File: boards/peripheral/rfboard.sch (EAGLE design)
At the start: 30 parts, among them Q1 IRLML5203, Q2 IRLML5203, Q3 IRLML5203, Q4 IRLML5203, Q5 IRLML5203

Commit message: Changing boards for fet and text improvements
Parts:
- removed Q5: IRLML5203, ngohara_parts:IRLML5203
- removed RGS: 2.2k, resistor:R-US_R0805
- removed RIN: 10k, resistor:R-US_R0805
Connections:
- removed net N$2: Q5.G, RGS.1, RIN.2
- net AMB_ON: no longer RIN.1
- net GND: no longer Q5.S, RGS.2
- net N_GND: no longer Q5.D
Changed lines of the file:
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@@
 <part name="U$1" library="jst-ph" deviceset="JST-PH10-SMD" device=""/>
 <part name="U$3" library="jst-ph" deviceset="JST-PH10-SMD" device=""/>
-<part name="Q5" library="ngohara_parts" deviceset="IRLML5203" device=""/>
 <part name="X1" library="con-molex-micro-fit-3_0" deviceset="HEADER_POS4_?" device="43045-0406"/>
-<part name="RIN" library="resistor" deviceset="R-US_" device="R0805" value="10k"/>
-<part name="RGS" library="resistor" deviceset="R-US_" device="R0805" value="2.2k"/>
 </parts>
 <sheets>
@@
 <instance part="U$1" gate="G$1" x="81.28" y="58.42" rot="MR180"/>
 <instance part="U$3" gate="G$1" x="53.34" y="55.88"/>
-<instance part="Q5" gate="G$1" x="137.16" y="104.14" smashed="yes" rot="R90">
-<attribute name="NAME" x="139.7" y="111.76" size="1.778" layer="95" rot="R180"/>
-</instance>
 <instance part="X1" gate="G$1" x="2.54" y="58.42" rot="R180"/>
-<instance part="RIN" gate="G$1" x="127" y="101.6"/>
-<instance part="RGS" gate="G$1" x="142.24" y="99.06"/>
 </instances>
 <busses>
@@
 </segment>
 <segment>
-<pinref part="Q5" gate="G$1" pin="S"/>
 <pinref part="GND10" gate="1" pin="GND"/>
-<wire x1="142.24" y1="106.68" x2="149.86" y2="106.68" width="0.1524" layer="91"/>
 <junction x="154.94" y="106.68"/>
-<junction x="142.24" y="106.68"/>
-<pinref part="RGS" gate="G$1" pin="2"/>
 <wire x1="149.86" y1="106.68" x2="154.94" y2="106.68" width="0.1524" layer="91"/>
-<wire x1="147.32" y1="99.06" x2="149.86" y2="99.06" width="0.1524" layer="91"/>
-<wire x1="149.86" y1="99.06" x2="149.86" y2="106.68" width="0.1524" layer="91"/>
-<junction x="147.32" y="99.06"/>
-<junction x="149.86" y="106.68"/>
 </segment>
 </net>
@@
 <wire x1="121.92" y1="101.6" x2="119.38" y2="101.6" width="0.1524" layer="91"/>
 <junction x="119.38" y="101.6"/>
-<pinref part="RIN" gate="G$1" pin="1"/>
-</segment>
-</net>
-<net name="N$2" class="0">
-<segment>
-<pinref part="Q5" gate="G$1" pin="G"/>
-<pinref part="RIN" gate="G$1" pin="2"/>
-<wire x1="132.08" y1="101.6" x2="134.62" y2="101.6" width="0.1524" layer="91"/>
-<wire x1="134.62" y1="101.6" x2="134.62" y2="99.06" width="0.1524" layer="91"/>
-<pinref part="RGS" gate="G$1" pin="1"/>
-<wire x1="134.62" y1="99.06" x2="137.16" y2="99.06" width="0.1524" layer="91"/>
-<junction x="134.62" y="101.6"/>
-<junction x="132.08" y="101.6"/>
-<junction x="137.16" y="99.06"/>
 </segment>
 </net>
@@
 <junction x="134.62" y="119.38"/>
 <junction x="149.86" y="124.46"/>
-<pinref part="Q5" gate="G$1" pin="D"/>
 <wire x1="132.08" y1="111.76" x2="132.08" y2="106.68" width="0.1524" layer="91"/>
-<junction x="132.08" y="106.68"/>
 <wire x1="147.32" y1="83.82" x2="165.1" y2="83.82" width="0.1524" layer="91"/>
 <wire x1="165.1" y1="83.82" x2="165.1" y2="111.76" width="0.1524" layer="91"/>

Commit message: fixed improper ground issue
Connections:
- removed net N_GND: AMB2.2, C1.2, OPT101.3, OPT101.8
- net GND: now also AMB2.2, C1.2, OPT101.3, OPT101.8
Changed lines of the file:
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@@
 <pinref part="GND10" gate="1" pin="GND"/>
 <junction x="154.94" y="106.68"/>
-<wire x1="149.86" y1="106.68" x2="154.94" y2="106.68" width="0.1524" layer="91"/>
+<pinref part="AMB2" gate="G$1" pin="2"/>
+<junction x="147.32" y="83.82"/>
+<pinref part="C1" gate="G$1" pin="2"/>
+<wire x1="121.92" y1="114.3" x2="121.92" y2="111.76" width="0.1524" layer="91"/>
+<wire x1="121.92" y1="111.76" x2="132.08" y2="111.76" width="0.1524" layer="91"/>
+<wire x1="132.08" y1="111.76" x2="165.1" y2="111.76" width="0.1524" layer="91"/>
+<wire x1="165.1" y1="111.76" x2="165.1" y2="124.46" width="0.1524" layer="91"/>
+<pinref part="OPT101" gate="G$1" pin="8"/>
+<wire x1="165.1" y1="124.46" x2="149.86" y2="124.46" width="0.1524" layer="91"/>
+<junction x="121.92" y="114.3"/>
+<junction x="132.08" y="111.76"/>
+<wire x1="132.08" y1="111.76" x2="132.08" y2="119.38" width="0.1524" layer="91"/>
+<pinref part="OPT101" gate="G$1" pin="3"/>
+<wire x1="132.08" y1="119.38" x2="134.62" y2="119.38" width="0.1524" layer="91"/>
+<junction x="134.62" y="119.38"/>
+<junction x="149.86" y="124.46"/>
+<wire x1="132.08" y1="111.76" x2="132.08" y2="106.68" width="0.1524" layer="91"/>
+<wire x1="147.32" y1="83.82" x2="165.1" y2="83.82" width="0.1524" layer="91"/>
+<wire x1="165.1" y1="83.82" x2="165.1" y2="111.76" width="0.1524" layer="91"/>
+<junction x="165.1" y="111.76"/>
+<wire x1="154.94" y1="106.68" x2="144.78" y2="106.68" width="0.1524" layer="91"/>
+<wire x1="132.08" y1="106.68" x2="139.7" y2="106.68" width="0.1524" layer="91"/>
+<wire x1="139.7" y1="106.68" x2="144.78" y2="106.68" width="0.1524" layer="91"/>
 </segment>
 </net>
@@
 </segment>
 </net>
-<net name="N_GND" class="1">
-<segment>
-<pinref part="AMB2" gate="G$1" pin="2"/>
-<junction x="147.32" y="83.82"/>
-<pinref part="C1" gate="G$1" pin="2"/>
-<wire x1="121.92" y1="114.3" x2="121.92" y2="111.76" width="0.1524" layer="91"/>
-<wire x1="121.92" y1="111.76" x2="132.08" y2="111.76" width="0.1524" layer="91"/>
-<wire x1="132.08" y1="111.76" x2="165.1" y2="111.76" width="0.1524" layer="91"/>
-<wire x1="165.1" y1="111.76" x2="165.1" y2="124.46" width="0.1524" layer="91"/>
-<pinref part="OPT101" gate="G$1" pin="8"/>
-<wire x1="165.1" y1="124.46" x2="149.86" y2="124.46" width="0.1524" layer="91"/>
-<junction x="121.92" y="114.3"/>
-<junction x="132.08" y="111.76"/>
-<wire x1="132.08" y1="111.76" x2="132.08" y2="119.38" width="0.1524" layer="91"/>
-<pinref part="OPT101" gate="G$1" pin="3"/>
-<wire x1="132.08" y1="119.38" x2="134.62" y2="119.38" width="0.1524" layer="91"/>
-<junction x="134.62" y="119.38"/>
-<junction x="149.86" y="124.46"/>
-<wire x1="132.08" y1="111.76" x2="132.08" y2="106.68" width="0.1524" layer="91"/>
-<wire x1="147.32" y1="83.82" x2="165.1" y2="83.82" width="0.1524" layer="91"/>
-<wire x1="165.1" y1="83.82" x2="165.1" y2="111.76" width="0.1524" layer="91"/>
-<junction x="165.1" y="111.76"/>
-</segment>
-</net>

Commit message: fixed PRF labels
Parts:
- AMB2: value 96k -> 200k
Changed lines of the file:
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@@
 <?xml version="1.0" encoding="utf-8"?>
 <!DOCTYPE eagle SYSTEM "eagle.dtd">
-<eagle version="6.4">
+<eagle version="6.5.0">
 <drawing>
 <settings>
@@
 <part name="U$2" library="jst-ph" deviceset="JST-PH2-SMD" device=""/>
 <part name="AMB1" library="resistor" deviceset="R-US_" device="R0805" value="200k"/>
-<part name="AMB2" library="resistor" deviceset="R-US_" device="R0805" value="96k"/>
+<part name="AMB2" library="resistor" deviceset="R-US_" device="R0805" value="200k"/>
 <part name="U$1" library="jst-ph" deviceset="JST-PH10-SMD" device=""/>
 <part name="U$3" library="jst-ph" deviceset="JST-PH10-SMD" device=""/>

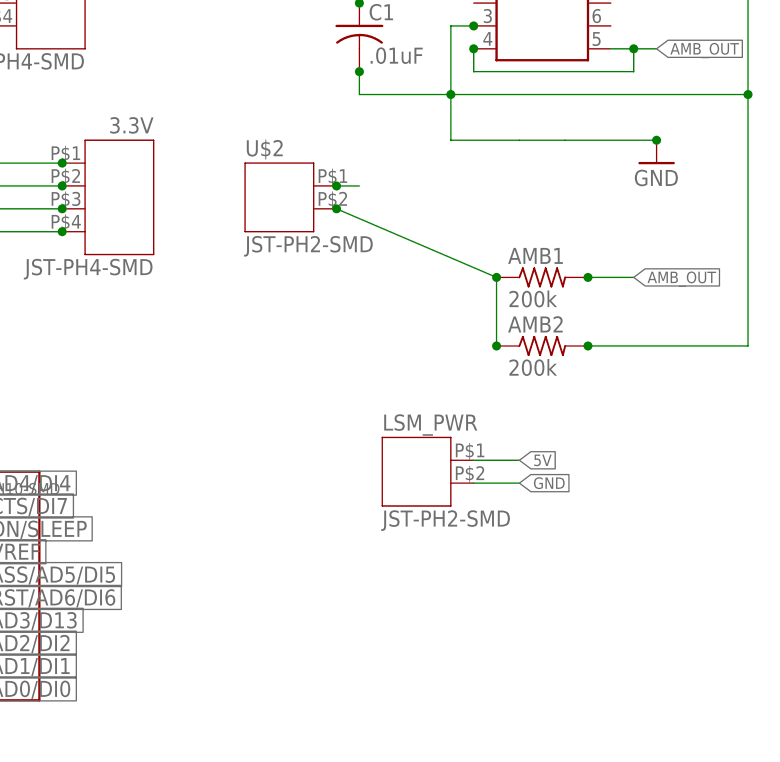
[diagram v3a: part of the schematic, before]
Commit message: changed size, moved holes, added servo header
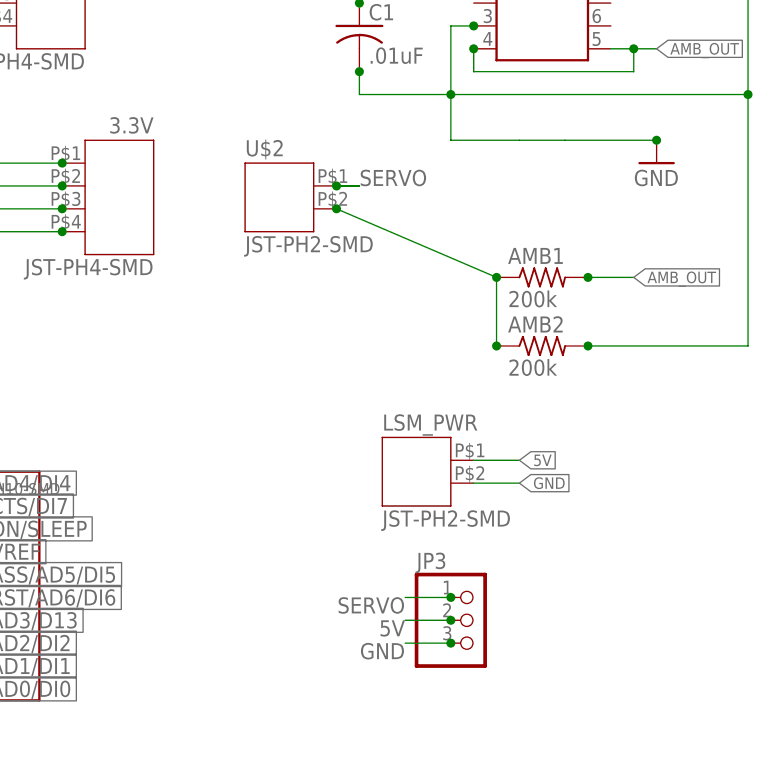
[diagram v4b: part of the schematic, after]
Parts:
- added JP3: (no value), pinhead:PINHD-1X3
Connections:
- removed net AMB_ON: U$2.1
- new net SERVO: JP3.1, U$2.1
- net 5V: now also JP3.2
- net GND: now also JP3.3
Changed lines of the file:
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@@
 <part name="U$3" library="jst-ph" deviceset="JST-PH10-SMD" device=""/>
 <part name="X1" library="con-molex-micro-fit-3_0" deviceset="HEADER_POS4_?" device="43045-0406"/>
+<part name="JP3" library="pinhead" deviceset="PINHD-1X3" device=""/>
 </parts>
 <sheets>
@@
 <instance part="U$3" gate="G$1" x="53.34" y="55.88"/>
 <instance part="X1" gate="G$1" x="2.54" y="58.42" rot="R180"/>
+<instance part="JP3" gate="A" x="134.62" y="53.34"/>
 </instances>
 <busses>
@@
 <wire x1="132.08" y1="106.68" x2="139.7" y2="106.68" width="0.1524" layer="91"/>
 <wire x1="139.7" y1="106.68" x2="144.78" y2="106.68" width="0.1524" layer="91"/>
+</segment>
+<segment>
+<wire x1="132.08" y1="50.8" x2="127" y2="50.8" width="0.1524" layer="91"/>
+<label x="127" y="50.8" size="1.778" layer="95" rot="R180"/>
+<pinref part="JP3" gate="A" pin="3"/>
+<junction x="132.08" y="50.8"/>
 </segment>
 </net>
@@
 <junction x="7.62" y="60.96"/>
 </segment>
+<segment>
+<wire x1="132.08" y1="53.34" x2="127" y2="53.34" width="0.1524" layer="91"/>
+<label x="127" y="53.34" size="1.778" layer="95" rot="R180"/>
+<pinref part="JP3" gate="A" pin="2"/>
+<junction x="132.08" y="53.34"/>
+</segment>
 </net>
 <net name="AD4/DI4" class="0">
@@
 </segment>
 </net>
-<net name="AMB_ON" class="0">
+<net name="SERVO" class="0">
+<segment>
+<wire x1="127" y1="55.88" x2="132.08" y2="55.88" width="0.1524" layer="91"/>
+<label x="127" y="55.88" size="1.778" layer="95" rot="R180"/>
+<pinref part="JP3" gate="A" pin="1"/>
+<junction x="132.08" y="55.88"/>
+</segment>
 <segment>
 <pinref part="U$2" gate="G$1" pin="1"/>
 <wire x1="121.92" y1="101.6" x2="119.38" y2="101.6" width="0.1524" layer="91"/>
 <junction x="119.38" y="101.6"/>
-</segment>
-</net>
+<wire x1="121.92" y1="101.6" x2="119.38" y2="101.6" width="0.1524" layer="91"/>
+<label x="121.92" y="101.6" size="1.778" layer="95"/>
+</segment>
+</net>
